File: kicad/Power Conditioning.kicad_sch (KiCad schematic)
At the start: 25 parts, among them J1 Conn_02x03_Odd_Even, U1 NCP1117-3.3_SOT223, U2 NCP1117-3.3_SOT223, U3 AP2171W, U4 AP2171W

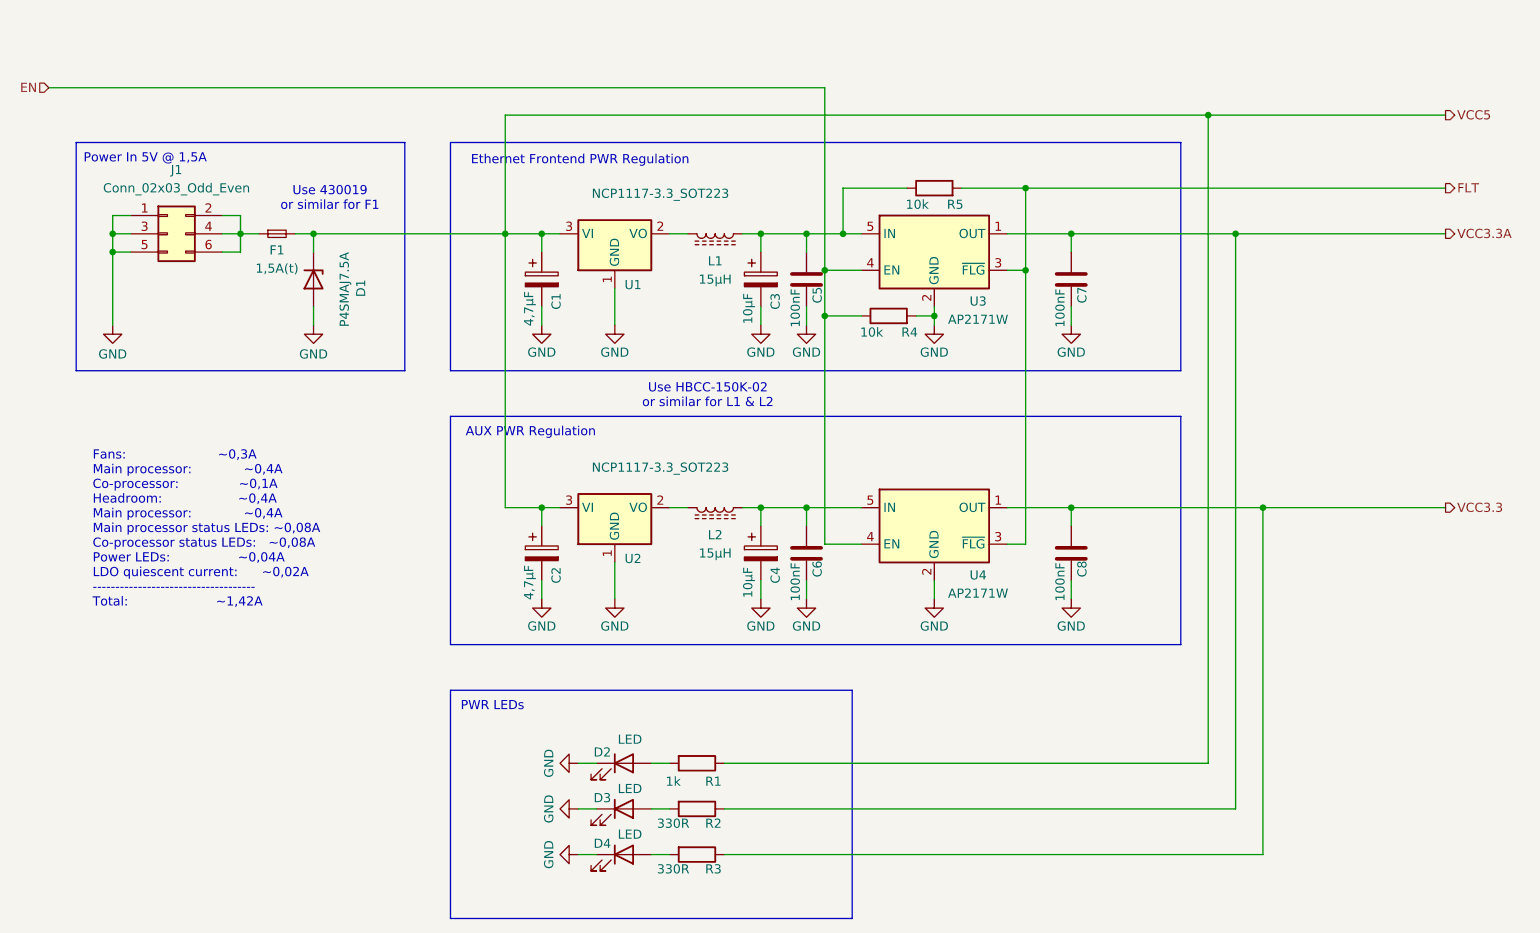
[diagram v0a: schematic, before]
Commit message: Add EtherKraken V1 Rev. C schematics as PDF to docs
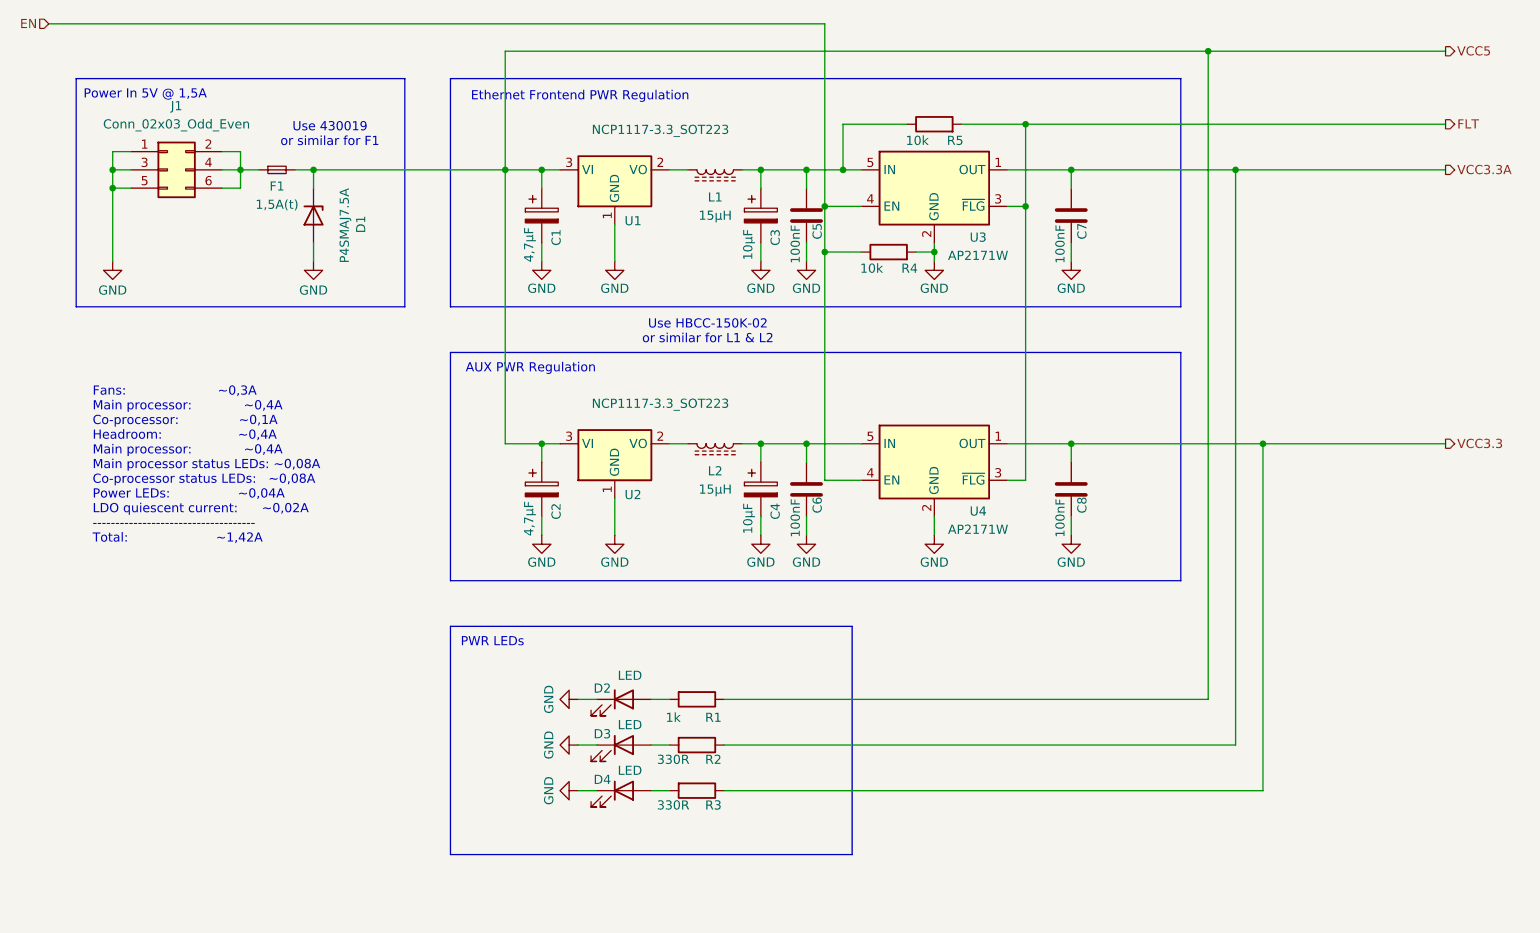
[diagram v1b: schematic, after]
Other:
- moved on the sheet: C1, C2, C3, C4, C5, C6, C7, C8, D1, D2, D3, D4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
